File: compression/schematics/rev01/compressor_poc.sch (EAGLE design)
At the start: 22 parts, among them IC1 TL084P

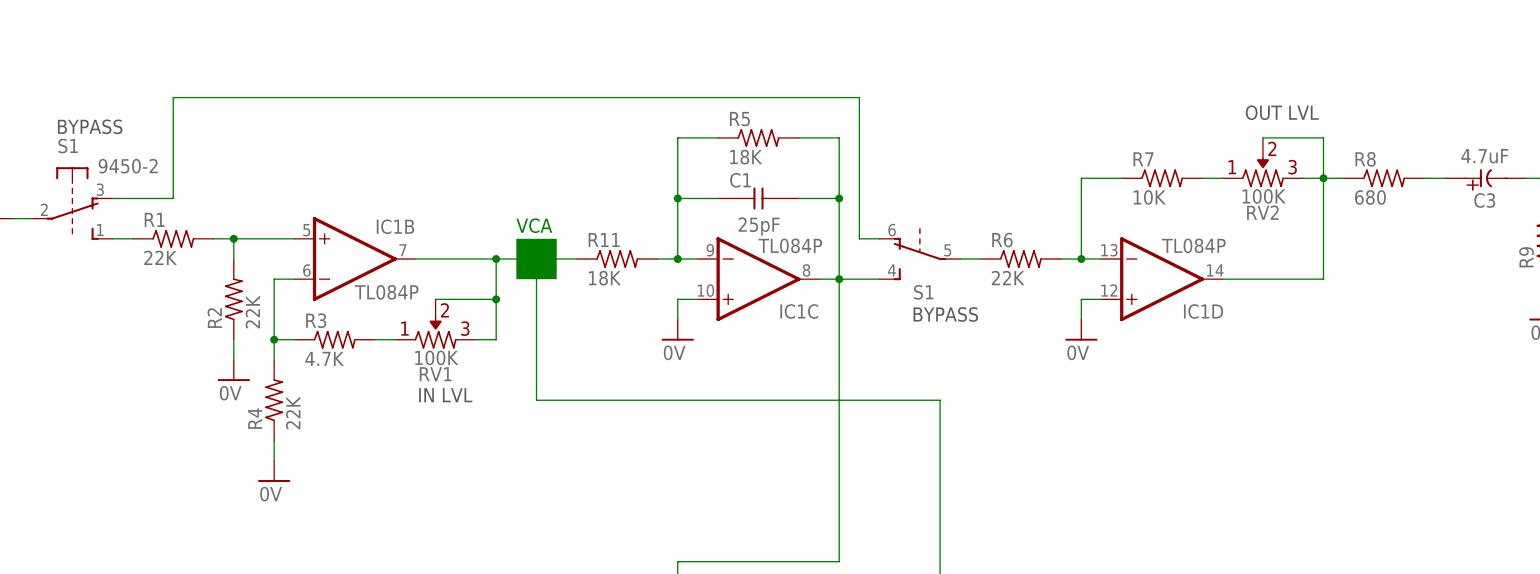
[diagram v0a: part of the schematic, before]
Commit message: Updated values from amp build
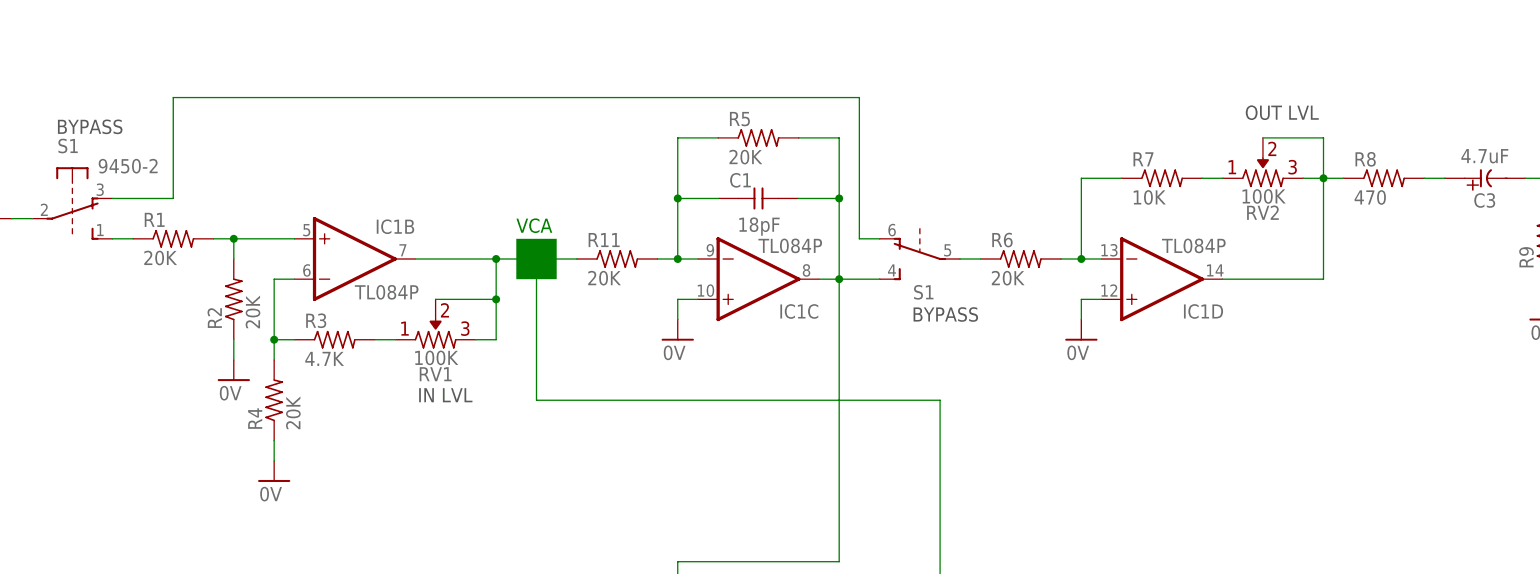
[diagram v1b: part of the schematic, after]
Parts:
- C1: value 25pF -> 18pF
- R1, R2, R4, R6: value 22K -> 20K
- R11, R5: value 18K -> 20K
- R8: value 680 -> 470
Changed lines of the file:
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@@
 <part name="P-1" library="supply1" library_urn="urn:adsk.eagle:library:371" deviceset="-12V" device=""/>
 <part name="GND1" library="supply1" library_urn="urn:adsk.eagle:library:371" deviceset="0V" device=""/>
-<part name="R1" library="rcl" library_urn="urn:adsk.eagle:library:334" deviceset="R-US_" device="0204/7" package3d_urn="urn:adsk.eagle:package:23498/2" value="22K"/>
-<part name="C1" library="_common.v1" deviceset="CC-US" device="025-024X044" value="25pF"/>
+<part name="R1" library="rcl" library_urn="urn:adsk.eagle:library:334" deviceset="R-US_" device="0204/7" package3d_urn="urn:adsk.eagle:package:23498/2" value="20K"/>
+<part name="C1" library="_common.v1" deviceset="CC-US" device="025-024X044" value="18pF"/>
 <part name="D1" library="diode" library_urn="urn:adsk.eagle:library:210" deviceset="1N4148" device="DO35-7" package3d_urn="urn:adsk.eagle:package:43339/2"/>
 <part name="J1" library="_common" deviceset="JACK-M" device=""/>
-<part name="R2" library="rcl" library_urn="urn:adsk.eagle:library:334" deviceset="R-US_" device="0204/7" package3d_urn="urn:adsk.eagle:package:23498/2" value="22K"/>
+<part name="R2" library="rcl" library_urn="urn:adsk.eagle:library:334" deviceset="R-US_" device="0204/7" package3d_urn="urn:adsk.eagle:package:23498/2" value="20K"/>
 <part name="R3" library="rcl" library_urn="urn:adsk.eagle:library:334" deviceset="R-US_" device="0204/7" package3d_urn="urn:adsk.eagle:package:23498/2" value="4.7K"/>
 <part name="C2" library="_common.v1" deviceset="CE-US" device="E2-5" value="4.7uF"/>
 <part name="S1" library="switch-misc" library_urn="urn:adsk.eagle:library:376" deviceset="9450-2" device="" package3d_urn="urn:adsk.eagle:package:27434/1"/>
 <part name="RV1" library="_common" deviceset="R-VAR" device="" value="100K"/>
-<part name="R4" library="rcl" library_urn="urn:adsk.eagle:library:334" deviceset="R-US_" device="0204/7" package3d_urn="urn:adsk.eagle:package:23498/2" value="22K"/>
+<part name="R4" library="rcl" library_urn="urn:adsk.eagle:library:334" deviceset="R-US_" device="0204/7" package3d_urn="urn:adsk.eagle:package:23498/2" value="20K"/>
 <part name="GND2" library="supply1" library_urn="urn:adsk.eagle:library:371" deviceset="0V" device=""/>
 <part name="GND3" library="supply1" library_urn="urn:adsk.eagle:library:371" deviceset="0V" device=""/>
-<part name="R5" library="rcl" library_urn="urn:adsk.eagle:library:334" deviceset="R-US_" device="0204/7" package3d_urn="urn:adsk.eagle:package:23498/2" value="18K"/>
+<part name="R5" library="rcl" library_urn="urn:adsk.eagle:library:334" deviceset="R-US_" device="0204/7" package3d_urn="urn:adsk.eagle:package:23498/2" value="20K"/>
 <part name="GND4" library="supply1" library_urn="urn:adsk.eagle:library:371" deviceset="0V" device=""/>
 <part name="RV2" library="_common" deviceset="R-VAR" device="" value="100K"/>
-<part name="R6" library="rcl" library_urn="urn:adsk.eagle:library:334" deviceset="R-US_" device="0204/7" package3d_urn="urn:adsk.eagle:package:23498/2" value="22K"/>
+<part name="R6" library="rcl" library_urn="urn:adsk.eagle:library:334" deviceset="R-US_" device="0204/7" package3d_urn="urn:adsk.eagle:package:23498/2" value="20K"/>
 <part name="R7" library="rcl" library_urn="urn:adsk.eagle:library:334" deviceset="R-US_" device="0204/7" package3d_urn="urn:adsk.eagle:package:23498/2" value="10K"/>
-<part name="R8" library="rcl" library_urn="urn:adsk.eagle:library:334" deviceset="R-US_" device="0204/7" package3d_urn="urn:adsk.eagle:package:23498/2" value="680"/>
+<part name="R8" library="rcl" library_urn="urn:adsk.eagle:library:334" deviceset="R-US_" device="0204/7" package3d_urn="urn:adsk.eagle:package:23498/2" value="470"/>
 <part name="C3" library="_common.v1" deviceset="CE-US" device="E2-5" value="4.7uF"/>
 <part name="J2" library="_common" deviceset="JACK-M" device=""/>
@@
 <part name="GND7" library="supply1" library_urn="urn:adsk.eagle:library:371" deviceset="0V" device=""/>
 <part name="GND8" library="supply1" library_urn="urn:adsk.eagle:library:371" deviceset="0V" device=""/>
-<part name="R11" library="rcl" library_urn="urn:adsk.eagle:library:334" deviceset="R-US_" device="0204/7" package3d_urn="urn:adsk.eagle:package:23498/2" value="18K"/>
+<part name="R11" library="rcl" library_urn="urn:adsk.eagle:library:334" deviceset="R-US_" device="0204/7" package3d_urn="urn:adsk.eagle:package:23498/2" value="20K"/>
 </parts>
 <sheets>

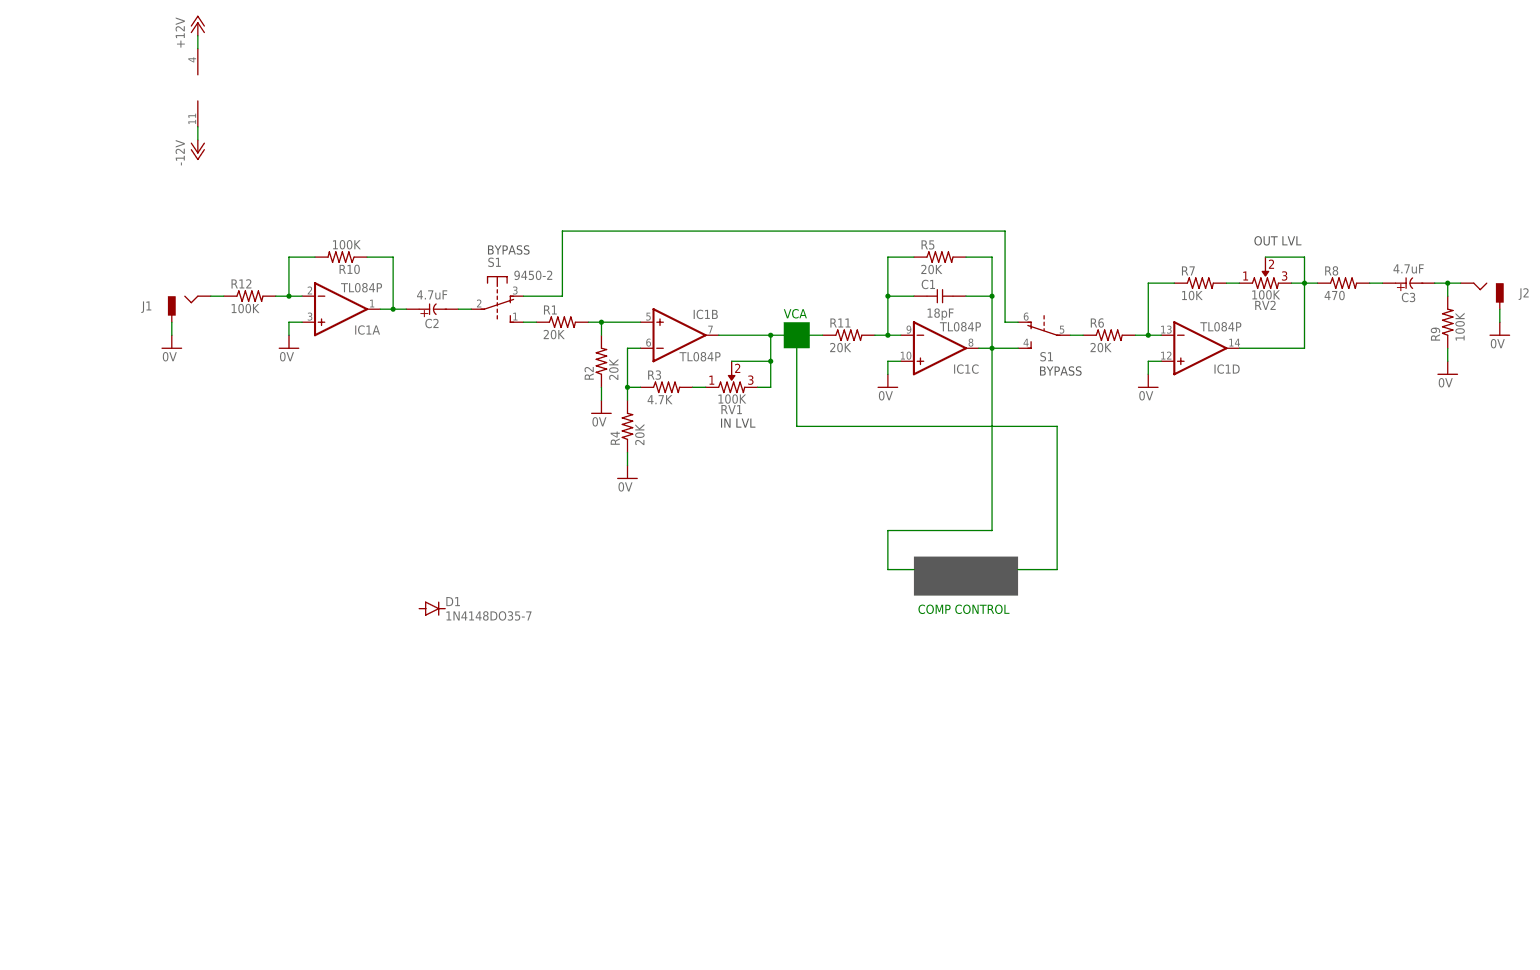
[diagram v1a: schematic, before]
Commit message: Added vca to compressor poc schem
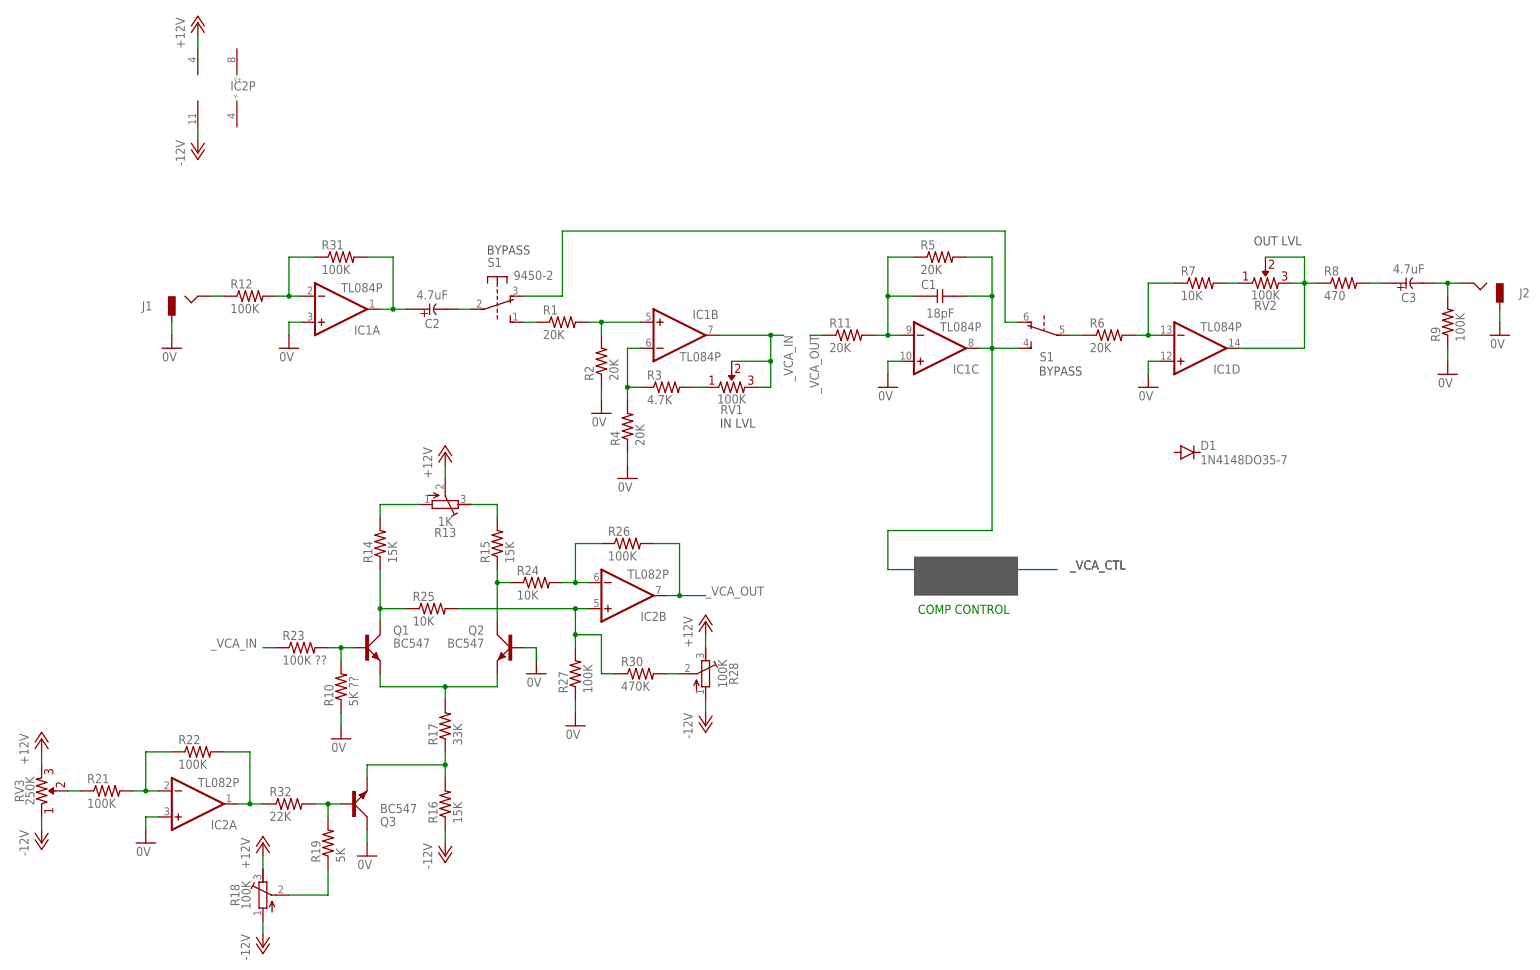
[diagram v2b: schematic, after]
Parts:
- added IC2: TL082P, _common:TL082P
- added Q1, Q2, Q3: BC547, transistor-small-signal:BC547
- added R13: 1K, _common:R-TRIMM3304W
- added R14, R15, R16: 15K, rcl:R-US_0204/7
- added R17: 33K, rcl:R-US_0204/7
- added R18, R28: 100K, _common:R-TRIMM3304W
- added R19: 5K, rcl:R-US_0204/7
- added R21, R22, R26, R27, R31: 100K, rcl:R-US_0204/7
- added R23: 100K ??, rcl:R-US_0204/7
- added R24, R25: 10K, rcl:R-US_0204/7
- added R30: 470K, rcl:R-US_0204/7
- added R32: 22K, rcl:R-US_0204/7
- added RV3: 250K, _common:R-VAR
- R10: value 100K -> 5K ??
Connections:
- new net N$20: R13.A, R15.2
- new net N$21: Q2.C, R15.1, R24.1
- new net N$22: Q1.C, R14.1, R25.1
- new net N$23: Q1.E, Q2.E, R17.2
- new net N$24: Q3.E, R16.2, R17.1
- new net N$25: Q3.B, R19.2, R32.2
- new net N$26: IC2A.OUT, R22.2, R32.1
- new net N$27: R18.S, R19.1
- new net N$28: IC2A.-IN, R21.2, R22.1
- new net N$29: R21.1, RV3.P$1
- new net N$30: Q1.B, R10.2, R23.2
- new net N$31: IC2B.+IN, R25.2, R27.2, R30.1
- new net N$32: R28.S, R30.2
- new net N$33: IC2B.-IN, R24.2, R26.1
- new net _VCA_IN: IC1B.OUT, R23.1, RV1.2, RV1.P$1
- new net _VCA_OUT: IC2B.OUT, R11.1, R26.2
- net +12V: now also R13.S, R18.A, R28.A, RV3.2
- net -12V: now also R16.1, R18.E, R28.E, RV3.1
- net 0V: now also IC2A.+IN, Q2.B, Q3.C, R10.1, R27.1
- net N$1: now also R13.E, R14.2; no longer IC1B.OUT, R11.1, RV1.2, RV1.P$1
- net N$16: now also R31.2; no longer R10.1
- net N$18: now also R31.1; no longer R10.2
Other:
- note removed: "VCA"
- moved on the sheet: D1, R10

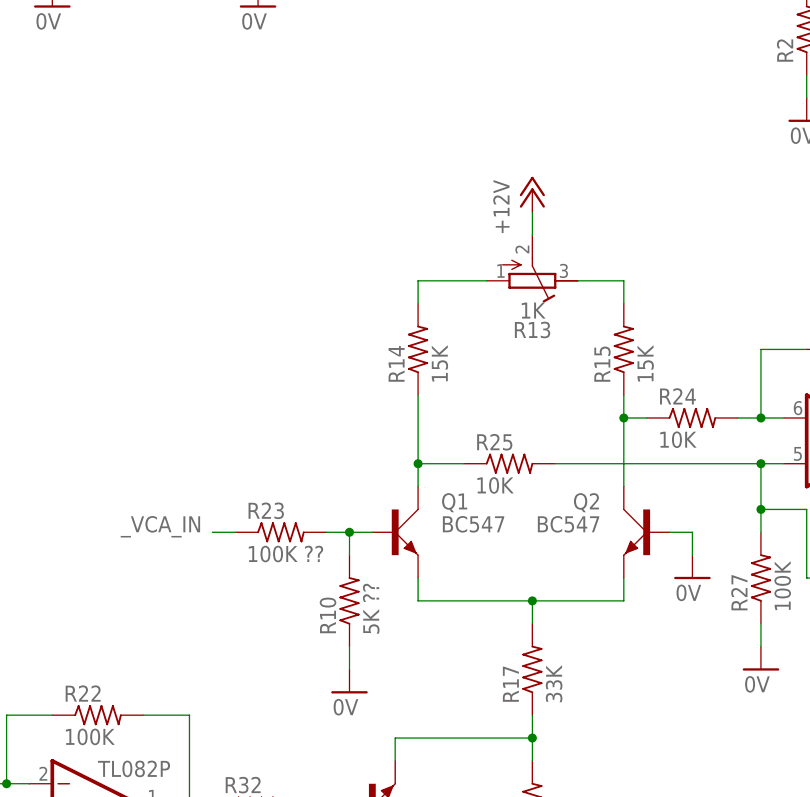
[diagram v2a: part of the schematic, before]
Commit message: Updated comp vca values from test build
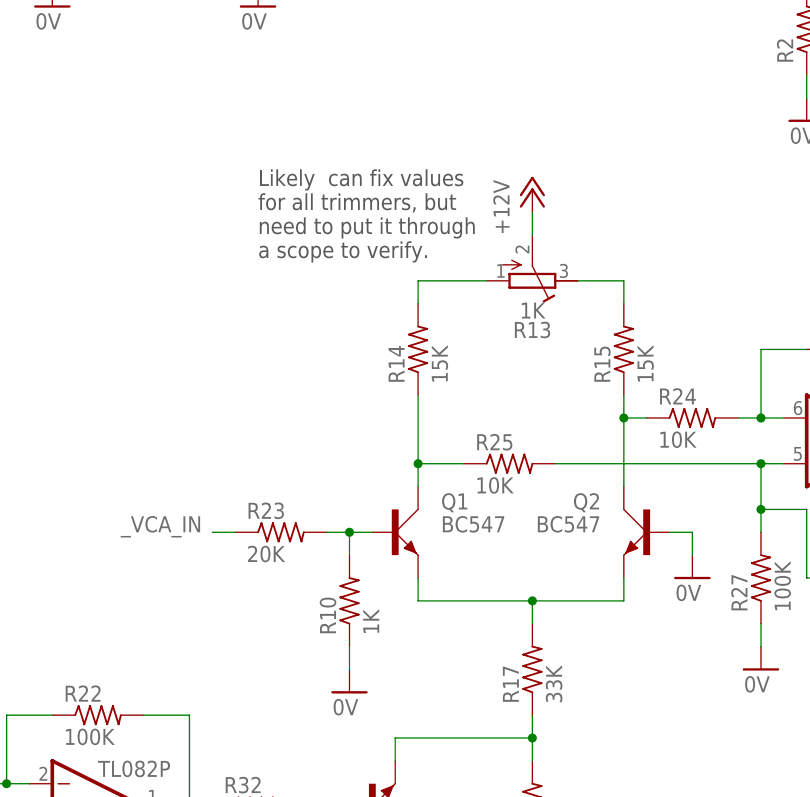
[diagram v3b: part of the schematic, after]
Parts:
- R10: value 5K ?? -> 1K
- R23: value 100K ?? -> 20K
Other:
- note added: "Likely can fix values for all trimmers, but need to put it through a scope to verify."
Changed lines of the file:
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@@
 <part name="P-4" library="supply1" library_urn="urn:adsk.eagle:library:371" deviceset="-12V" device=""/>
 <part name="GND10" library="supply1" library_urn="urn:adsk.eagle:library:371" deviceset="0V" device=""/>
-<part name="R23" library="rcl" library_urn="urn:adsk.eagle:library:334" deviceset="R-US_" device="0204/7" package3d_urn="urn:adsk.eagle:package:23498/2" value="100K ??"/>
+<part name="R23" library="rcl" library_urn="urn:adsk.eagle:library:334" deviceset="R-US_" device="0204/7" package3d_urn="urn:adsk.eagle:package:23498/2" value="20K"/>
 <part name="GND11" library="supply1" library_urn="urn:adsk.eagle:library:371" deviceset="0V" device=""/>
 <part name="R24" library="rcl" library_urn="urn:adsk.eagle:library:334" deviceset="R-US_" device="0204/7" package3d_urn="urn:adsk.eagle:package:23498/2" value="10K"/>
@@
 <part name="R31" library="rcl" library_urn="urn:adsk.eagle:library:334" deviceset="R-US_" device="0204/7" package3d_urn="urn:adsk.eagle:package:23498/2" value="100K"/>
 <part name="R32" library="rcl" library_urn="urn:adsk.eagle:library:334" deviceset="R-US_" device="0204/7" package3d_urn="urn:adsk.eagle:package:23498/2" value="22K"/>
-<part name="R10" library="rcl" library_urn="urn:adsk.eagle:library:334" deviceset="R-US_" device="0204/7" package3d_urn="urn:adsk.eagle:package:23498/2" value="5K ??"/>
+<part name="R10" library="rcl" library_urn="urn:adsk.eagle:library:334" deviceset="R-US_" device="0204/7" package3d_urn="urn:adsk.eagle:package:23498/2" value="1K"/>
 <part name="GND13" library="supply1" library_urn="urn:adsk.eagle:library:371" deviceset="0V" device=""/>
 </parts>
@@
 <text x="137.922" y="21.844" size="1.778" layer="91">COMP CONTROL</text>
 <rectangle x1="137.16" y1="25.4" x2="157.48" y2="33.02" layer="97"/>
+<text x="15.24" y="45.72" size="1.778" layer="97">Likely  can fix values
+for all trimmers, but
+need to put it through
+a scope to verify.</text>
 </plain>
 <instances>
@@
 </drawing>
 <compatibility>
+<note version="6.3" minversion="6.2.2" severity="warning">
+Since Version 6.2.2 text objects can contain more than one line,
+which will not be processed correctly with this version.
+</note>
 <note version="8.2" severity="warning">
 Since Version 8.2, EAGLE supports online libraries. The ids
